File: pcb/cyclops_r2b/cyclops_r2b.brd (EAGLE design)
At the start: 132.2 x 81.4 mm, 52 parts, among them IC2 317, IC3 REF02Z, IC5 LM324N

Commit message: Changed filter network resistor values to 0R to indicate application dependence.
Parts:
- R3, R4: value 10k -> 0R
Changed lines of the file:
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@@
 </element>
 <element name="IC3" library="linear" package="DIL08" value="REF02Z" x="38.4175" y="28.575"/>
-<element name="R3" library="HOSS" package="0207/7" value="10k" x="28.2575" y="28.575" rot="R90"/>
-<element name="R4" library="HOSS" package="0207/7" value="10k" x="23.1775" y="28.575" rot="R90"/>
+<element name="R3" library="HOSS" package="0207/7" value="0R" x="28.2575" y="28.575" rot="R90"/>
+<element name="R4" library="HOSS" package="0207/7" value="0R" x="23.1775" y="28.575" rot="R90"/>
 <element name="JP3" library="jumper" package="JP1" value="" x="58.42" y="37.1475" smashed="yes" rot="R270">
 <attribute name="NAME" x="58.1025" y="34.3535" size="1.27" layer="25" ratio="10"/>

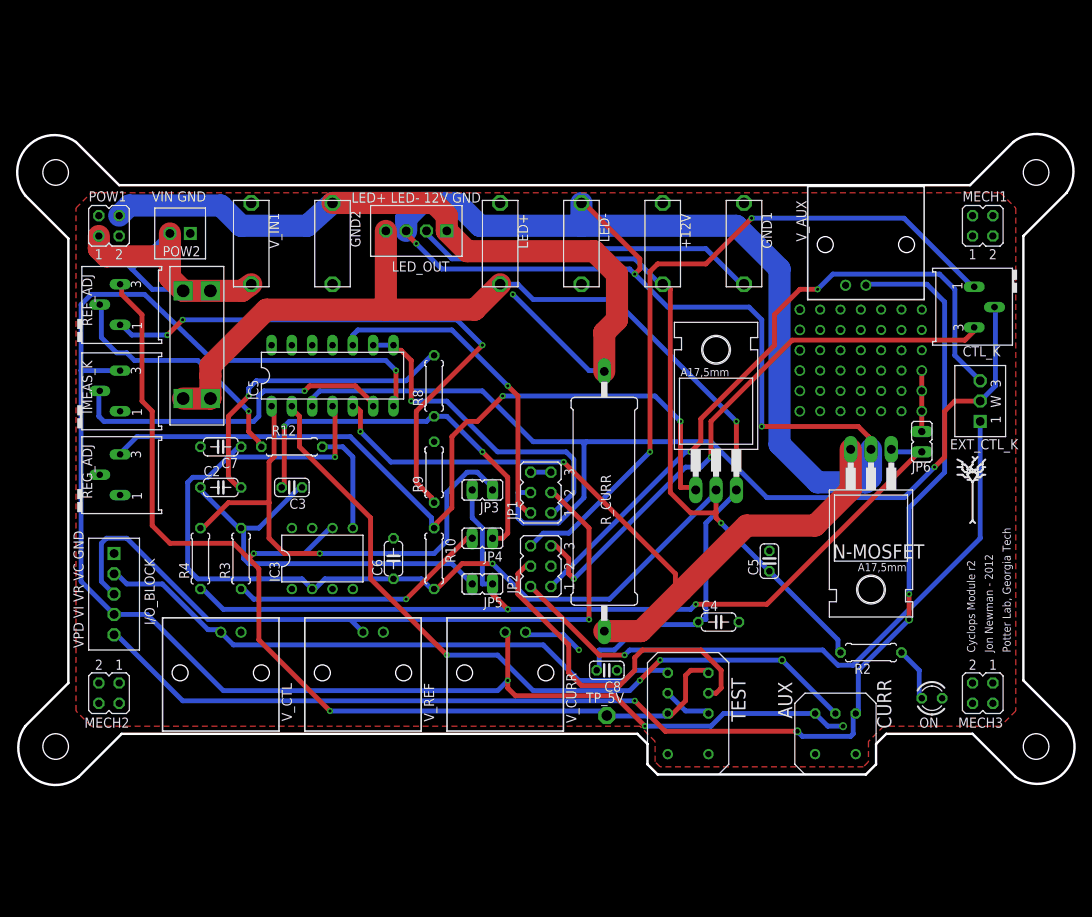
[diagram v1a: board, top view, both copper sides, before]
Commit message: Fixed r2b in terms of extra traces, ground plane islands, and added extra tuning resistor that was available in r0, but was removed in r2.
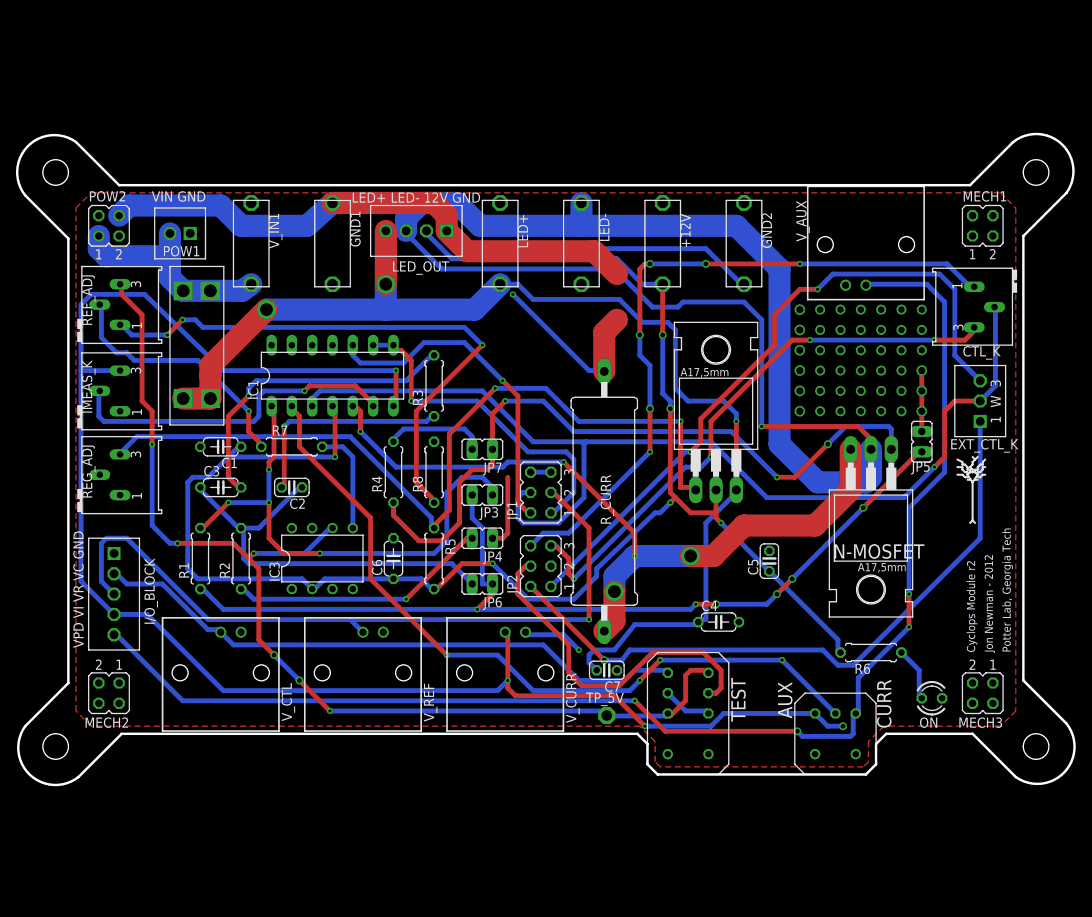
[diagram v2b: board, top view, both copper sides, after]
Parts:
- removed C8: 10u, rcl:C025-024X044
- removed R9: 1k, HOSS:0207/7
- added C1: 0.1uF, rcl:C050-024X044
- added JP7: (no value), jumper:JP1
- added R1: 0R, HOSS:0207/7
- added R6: 1.5k, HOSS:0207/7
- C2: value 0.1uF -> 1.0uF; device rcl:C050-024X044 -> rcl:C025-024X044
- C3: value 1.0uF -> 0.1uF; device rcl:C025-024X044 -> rcl:C050-024X044
- C7: value 0.1uF -> 10u; device rcl:C050-024X044 -> rcl:C025-024X044
- POW1: value (none) -> SCREW2; device jumper:JP2Q -> HOSS:SCREW2
- POW2: value SCREW2 -> (none); device HOSS:SCREW2 -> jumper:JP2Q
- R2: value 1.5k -> 0R
- R3: value 0R -> 120
- R8: value 120 -> 1k
- moved R2 79.6 mm to (28.3, 28.6), turned to 90 degrees
- moved JP5 57.7 mm to (113.3, 43.2), turned to 180 degrees
- moved JP6 57.7 mm to (58.4, 25.4), turned to 90 degrees
- moved C7 55.8 mm to (74.0, 14.6)
- moved GND1 52.4 mm to (39.7, 73.0), turned to 270 degrees
- moved GND2 52.4 mm to (91.1, 62.9), turned to 90 degrees
- moved R3 32.4 mm to (52.4, 50.2)
- moved R4 26.4 mm to (47.3, 39.4)
- moved R8 10.8 mm to (52.4, 39.4)
- moved POW1 10.2 mm to (21.9, 69.2), turned to 180 degrees
- moved POW2 10.2 mm to (11.7, 70.2), turned to 0 degrees
- moved C2 8.89 mm to (34.6, 37.5), turned to 180 degrees
- moved C3 8.89 mm to (25.7, 37.5), turned to 0 degrees
- moved JP3 0.63 mm to (58.4, 36.5)
- renumbered IC5 to IC1, R10 to R5, R12 to R7
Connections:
- new net N$16: JP7.2, R4.2
- new net N$30: JP7.1, N-MOSFET.G, R4.1
- net GND: now also C1.2, C2.2, C7.1, POW1.P$1, POW2.4, R3.1, R8.2; no longer C3.2, C7.2, C8.1, POW1.4, POW2.P$1, R8.1, R9.2
- net N$11: now also JP6.2, R2.2; no longer JP5.2, R3.2
- net N$13: now also C3.2, R3.2; no longer C2.2, R8.2
- net N$24: now also R8.1; no longer R9.1
- net N$27: now also R2.1; no longer R3.1
- net N$28: now also R6.1; no longer R2.1
- net N$29: now also JP5.2, JP6.1, R1.1; no longer JP5.1, JP6.2, N-MOSFET.G, R4.1
- net N$3: now also R1.2; no longer R4.2
- net N$69: now also JP5.1; no longer JP6.1
- net P_12V: now also C1.1, R6.2; no longer C7.1, R2.2
- net P_SUP: now also C7.2; no longer C8.2
- net P_SUP_BEFORE: now also POW1.P$2, POW2.1; no longer POW1.1, POW2.P$2
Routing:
- net N$30: track 0.00 -> 88.3 mm, vias 0 -> 3
- net P_SUP_BEFORE: track 56.6 -> 27.2 mm
- net GND: track 195.5 -> 177.5 mm, vias 10 -> 9
- net N$16: track 0.00 -> 12.7 mm
- net N$21: track 184.9 -> 173.1 mm, vias 3 -> 1
- net P_12V: track 209.1 -> 204.3 mm, vias 3 -> 6
- net N$29: track 120.8 -> 116.2 mm, vias 2 -> 6
- net N$2: track 96.1 -> 93.1 mm, vias 2 -> 5
- net N$12: track 89.1 -> 86.4 mm, vias 2 -> 6
- net P_SUP: track 144.2 -> 146.2 mm, vias 1 -> 3
- net N$6: track 44.9 -> 43.7 mm
- net N$19: track 100.7 -> 101.9 mm
- net N$25: track 82.0 -> 82.6 mm
- net N$14: track 41.0 -> 41.6 mm
- net N$3: track 64.6 -> 64.7 mm, vias 1 -> 4
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
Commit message: Finished revision 2b. Sent for fabrication.
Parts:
- IC3: value REF02Z -> REF02; device linear:DIL08 -> linear:DIL08-OVAL
- moved C1 14.0 mm to (39.7, 43.2), turned to 0 degrees
- moved R7 7.62 mm to (27.0, 42.5)
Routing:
- net GND: track 177.5 -> 134.8 mm, vias 9 -> 7
- net N$4: track 199.8 -> 195.7 mm, vias 4 -> 3
- net N$7: track 71.9 -> 68.1 mm, vias 4 -> 5
- net N$20: track 13.5 -> 16.5 mm
- net P_12V: track 204.3 -> 202.1 mm, vias 6 -> 5
- net N$2: track 93.1 -> 95.0 mm
- net REF_5V: track 133.3 -> 135.0 mm, vias 6 -> 8
- net N$16: track 12.7 -> 14.2 mm
- net N$13: track 39.2 -> 37.7 mm, vias 1 -> 2
- net N$29: track 116.2 -> 117.3 mm
- net N$27: track 32.6 -> 33.6 mm
- net N$18: track 92.7 -> 91.8 mm
- net N$19: track 101.9 -> 102.5 mm
- net N$24: track 72.1 -> 71.9 mm, vias 3 -> 5
- net N$1: vias 4 -> 6

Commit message: Fixed several problems with r2b.
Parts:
- +12V, GND1, GND2, LED+, LED-, V_IN1: device HOSS:BANANA_TO_BOARD -> cyclops:BANANA_TO_BOARD
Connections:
- removed net N$16: JP7.2, R4.2
- net GND: now also GND1.P$2, GND2.P$2
- net N$21: now also LED-.P$2
- net N$29: now also JP7.2, R4.2
- net P_12V: now also +12V.P$2
- net P_SUP: now also LED+.P$2
- net P_SUP_BEFORE: now also V_IN1.P$2
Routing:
- net GND: track 134.8 -> 9.15 mm, vias 7 -> 6
- net N$29: track 117.3 -> 144.6 mm, vias 6 -> 7
- net N$16: track 14.2 -> 0.00 mm
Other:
- board text added: "Cyclops Module r2b"
- board text added: "V_CTL"
- board text added: "V_CURR"
- board text added: "V_REF"
- board text removed: "Cyclops Module r2"

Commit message: Ready for printing.
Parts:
- V_AUX, V_CTL, V_CURR, V_REF: device con-coax:AMP_227161 -> cyclops:AMP_227161
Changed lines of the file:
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@@
 <attribute name="VALUE" x="36.3855" y="40.132" size="1.27" layer="27" font="vector" ratio="10" rot="R180"/>
 </element>
-<element name="V_CURR" library="con-coax" package="AMP_227161" value="1-227161-0" x="61.2775" y="14.2875" smashed="yes" rot="R180">
+<element name="V_CURR" library="cyclops" package="AMP_227161" value="1-227161-0" x="61.2775" y="14.2875" smashed="yes" rot="R180">
 <attribute name="NAME" x="68.8975" y="14.2875" size="1.27" layer="25" font="vector" rot="R270"/>
-<attribute name="OC_NEWARK" value="33B3200" x="61.2775" y="14.2875" size="1.778" layer="27" rot="R180" display="off"/>
-<attribute name="MPN" value="1-227161" x="61.2775" y="14.2875" size="1.778" layer="27" rot="R180" display="off"/>
-<attribute name="MF" value="TYCO ELECTRONICS" x="61.2775" y="14.2875" size="1.778" layer="27" rot="R180" display="off"/>
-<attribute name="OC_FARNELL" value="unknown" x="61.2775" y="14.2875" size="1.778" layer="27" rot="R180" display="off"/>
 </element>
-<element name="V_CTL" library="con-coax" package="AMP_227161" value="1-227161-0" x="25.7175" y="14.2875" smashed="yes" rot="R180">
+<element name="V_CTL" library="cyclops" package="AMP_227161" value="1-227161-0" x="25.7175" y="14.2875" smashed="yes" rot="R180">
 <attribute name="NAME" x="33.3375" y="13.0175" size="1.27" layer="25" font="vector" rot="R270"/>
-<attribute name="OC_NEWARK" value="33B3200" x="25.7175" y="14.2875" size="1.778" layer="27" rot="R180" display="off"/>
-<attribute name="MPN" value="1-227161" x="25.7175" y="14.2875" size="1.778" layer="27" rot="R180" display="off"/>
-<attribute name="MF" value="TYCO ELECTRONICS" x="25.7175" y="14.2875" size="1.778" layer="27" rot="R180" display="off"/>
-<attribute name="OC_FARNELL" value="unknown" x="25.7175" y="14.2875" size="1.778" layer="27" rot="R180" display="off"/>
 </element>
 <element name="IC1" library="linear" package="DIL14" value="LM324N" x="39.6875" y="51.435" smashed="yes">
@@
 <attribute name="VALUE" x="32.9565" y="50.8" size="1.27" layer="27" font="vector" ratio="10"/>
 </element>
-<element name="V_REF" library="con-coax" package="AMP_227161" value="1-227161-0" x="43.4975" y="14.2875" smashed="yes" rot="R180">
+<element name="V_REF" library="cyclops" package="AMP_227161" value="1-227161-0" x="43.4975" y="14.2875" smashed="yes" rot="R180">
 <attribute name="NAME" x="51.1175" y="13.0175" size="1.27" layer="25" font="vector" rot="R270"/>
-<attribute name="OC_NEWARK" value="33B3200" x="43.4975" y="14.2875" size="1.778" layer="27" rot="R180" display="off"/>
-<attribute name="MPN" value="1-227161" x="43.4975" y="14.2875" size="1.778" layer="27" rot="R180" display="off"/>
-<attribute name="MF" value="TYCO ELECTRONICS" x="43.4975" y="14.2875" size="1.778" layer="27" rot="R180" display="off"/>
-<attribute name="OC_FARNELL" value="unknown" x="43.4975" y="14.2875" size="1.778" layer="27" rot="R180" display="off"/>
 </element>
-<element name="V_AUX" library="con-coax" package="AMP_227161" value="1-227161-0" x="106.3625" y="67.818" smashed="yes">
+<element name="V_AUX" library="cyclops" package="AMP_227161" value="1-227161-0" x="106.3625" y="67.818" smashed="yes">
 <attribute name="NAME" x="97.663" y="73.3425" size="1.27" layer="25" font="vector" rot="R270"/>
-<attribute name="OC_NEWARK" value="33B3200" x="106.3625" y="67.818" size="1.778" layer="27" display="off"/>
-<attribute name="MPN" value="1-227161" x="106.3625" y="67.818" size="1.778" layer="27" display="off"/>
-<attribute name="MF" value="TYCO ELECTRONICS" x="106.3625" y="67.818" size="1.778" layer="27" display="off"/>
-<attribute name="OC_FARNELL" value="unknown" x="106.3625" y="67.818" size="1.778" layer="27" display="off"/>
 </element>
 <element name="IC3" library="linear" package="DIL08-OVAL" value="REF02" x="38.4175" y="28.575" smashed="yes">

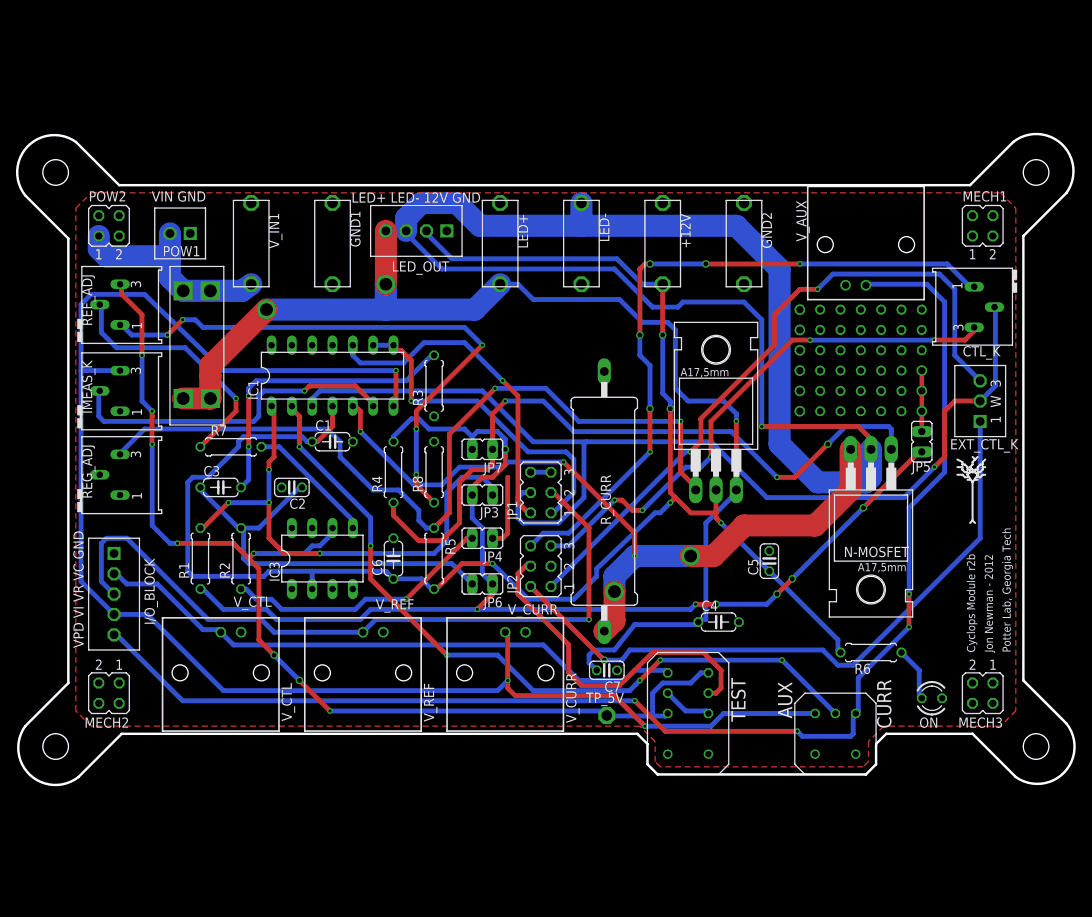
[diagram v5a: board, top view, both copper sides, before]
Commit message: Revision 2b of the cyclops driver, ready for OSH Park.
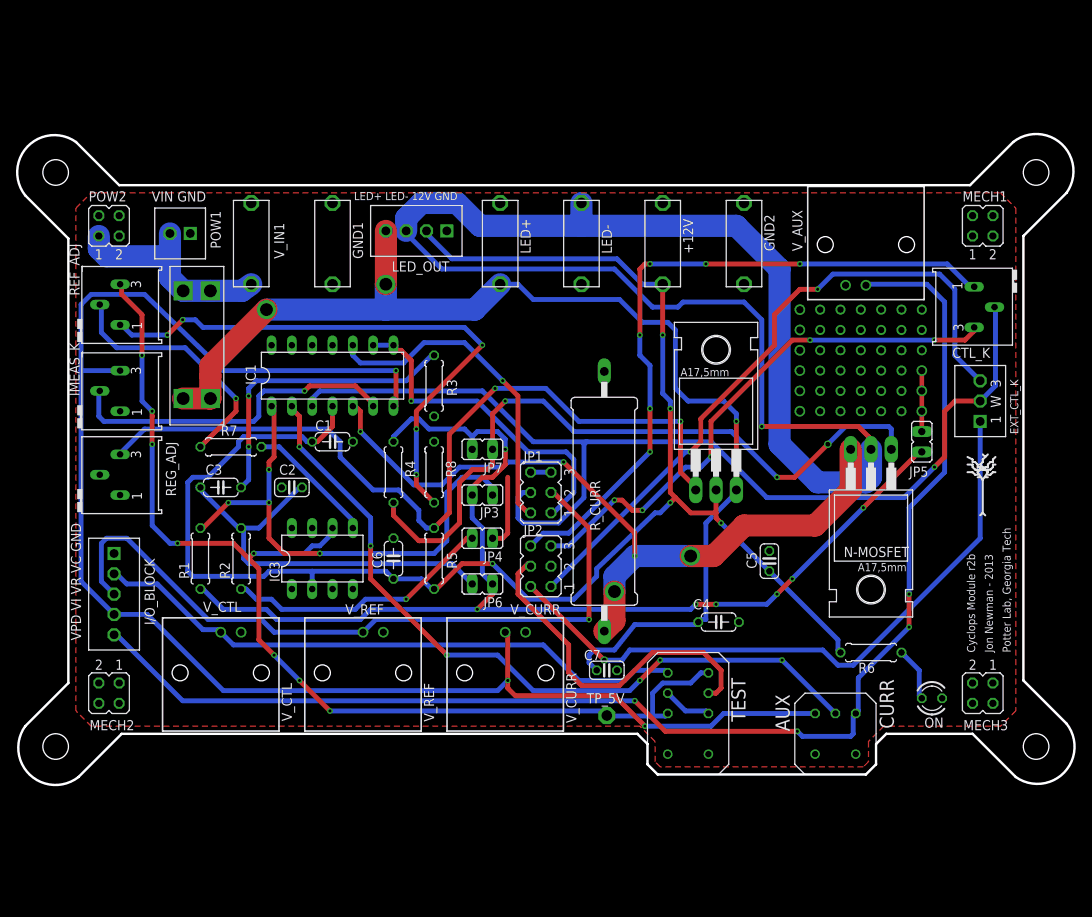
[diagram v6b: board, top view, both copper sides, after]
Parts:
- added U$2: (no value), ohw-logo:OSHW_FILLX750_NOTEXT
- C7: value 10u -> 10uF
- CTL_K, IMEAS_K, REF_ADJ, REG_ADJ: device HOSS:RJ6S -> cyclops:RJ6S
- R_CURR: device HOSS:IMEAS_R -> cyclops:IMEAS_R
- TP_5V: value TPPAD1-13 -> (none)
- U$1: device HOSS:NXT-FUSE -> cyclops:NXT-FUSE
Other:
- board text added: "Jon Newman - 2013"
- board text added: "S/N:"
- board text removed: "Jon Newman - 2012"
